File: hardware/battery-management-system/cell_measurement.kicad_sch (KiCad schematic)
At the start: 29 parts, among them Q10 DMN3404L, Q11 BS250FTA, Q12 BS250FTA, Q13 BS250FTA, Q14 BS250FTA, Q15 BS250FTA, Q9 DMN3404L, U10 LM2904M8-13, U9 LM2904M8-13

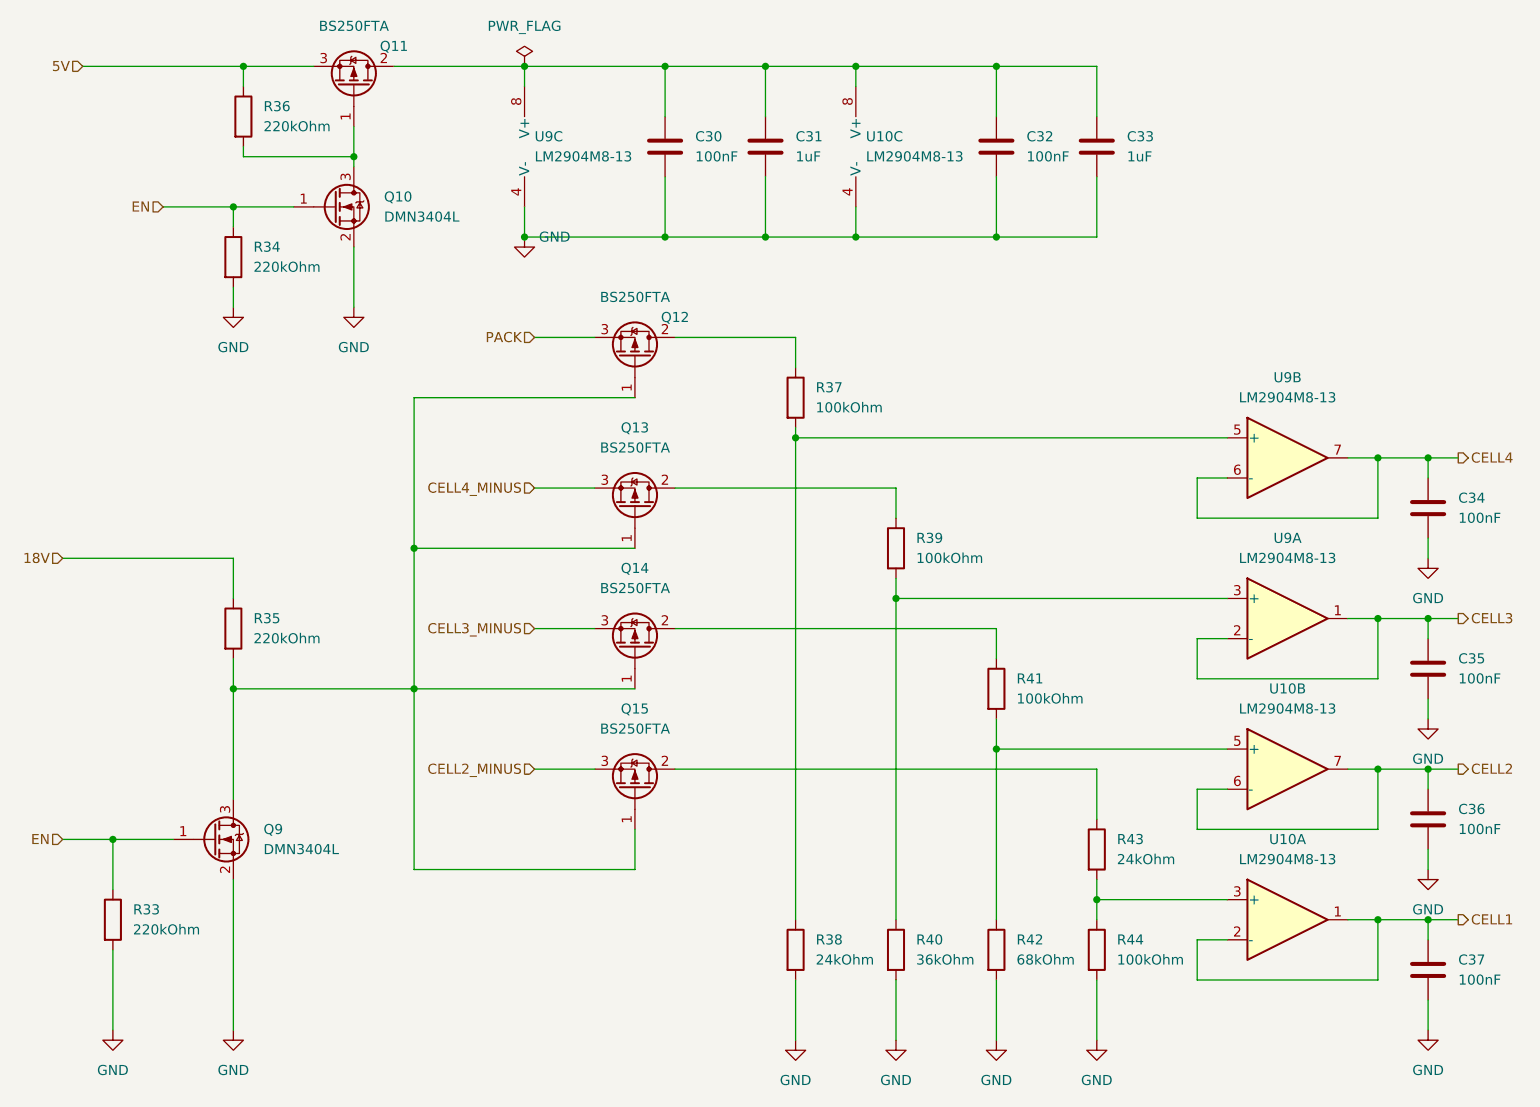
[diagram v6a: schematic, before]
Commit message: add snubber circuit
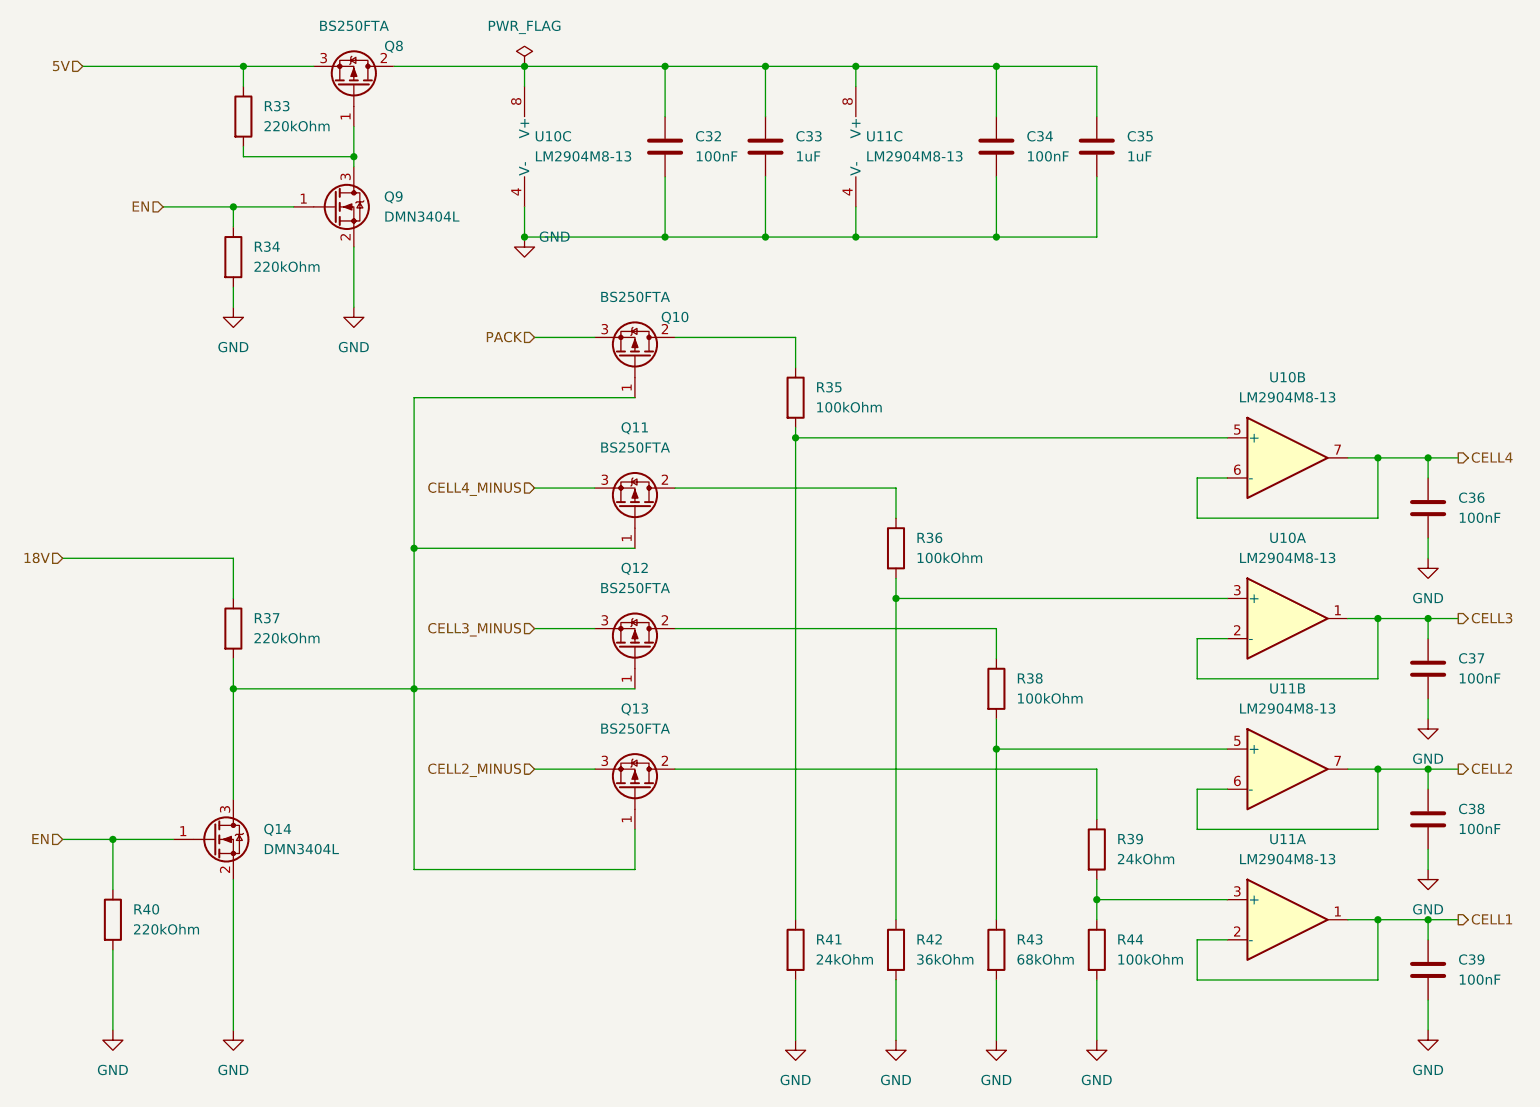
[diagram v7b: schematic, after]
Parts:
- renumbered C30 to C32, C31 to C33, C32 to C34, C33 to C35, C34 to C36, C35 to C37, C36 to C38, C37 to C39, Q12 to Q10, Q13 to Q11, Q14 to Q12, Q15 to Q13, Q9 to Q14, Q11 to Q8, Q10 to Q9, R36 to R33, R37 to R35, R39 to R36, R35 to R37, R41 to R38, R43 to R39, R33 to R40, R38 to R41, R40 to R42, R42 to R43, U9 to U10, U10 to U11
